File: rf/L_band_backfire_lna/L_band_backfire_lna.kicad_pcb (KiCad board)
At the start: 2 copper layers, 42.6 x 42.6 mm, 24 parts, among them J1 SMA, J2 SMA, U1 QPL9547, U2 QPL9547, X1 SAW, X2 SAW

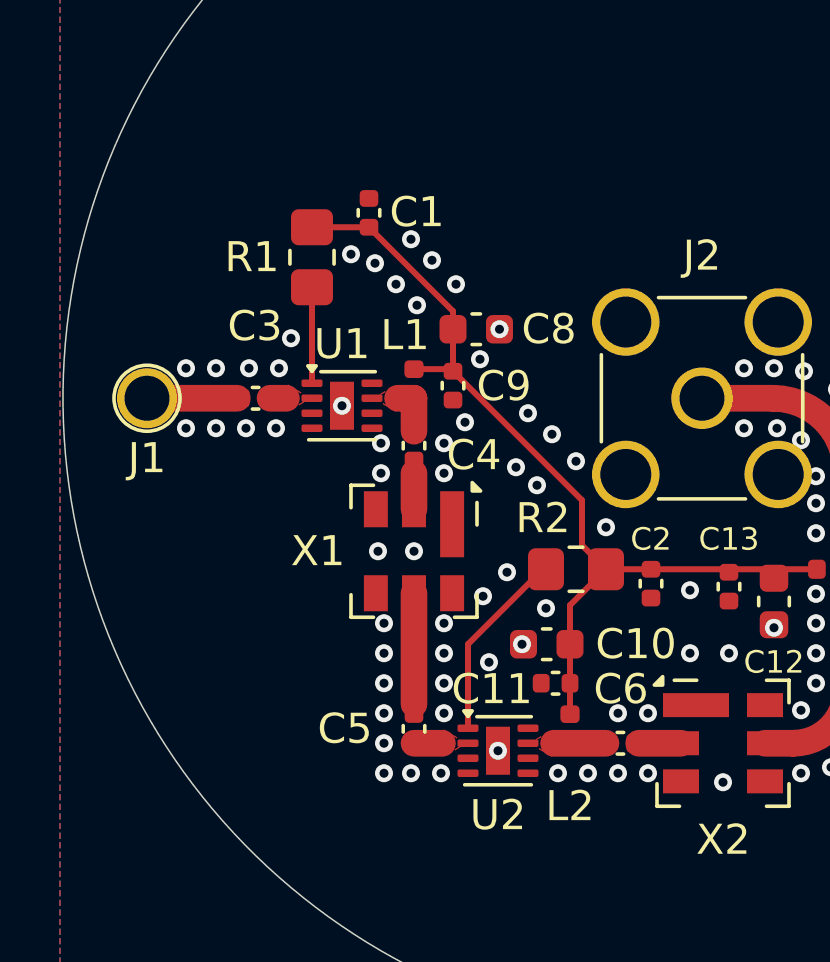
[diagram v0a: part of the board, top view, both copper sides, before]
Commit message: Make curves smoother
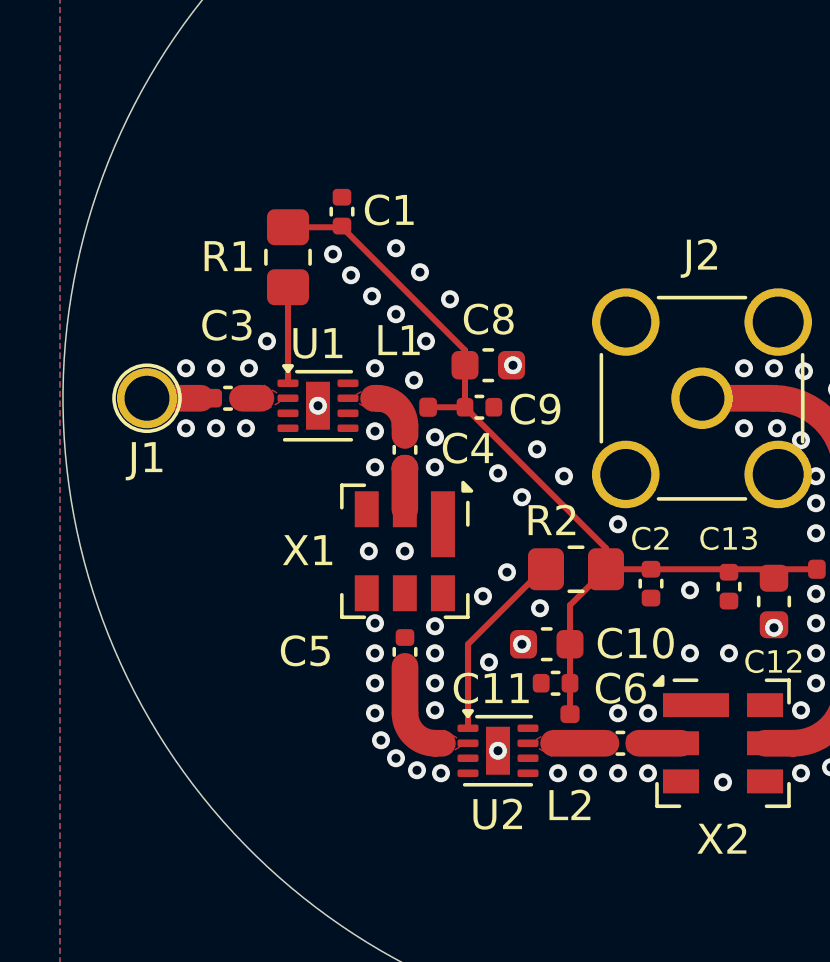
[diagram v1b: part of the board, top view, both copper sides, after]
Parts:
- moved C5 2.58 mm to (140.1, 108.5)
- moved C8 1.26 mm to (142.9, 98.9)
- moved C9 1.14 mm to (142.6, 100.3), turned to 180 degrees
- moved C3 0.92 mm to (134.2, 100.0)
- moved C1 0.90 mm to (138.0, 93.8)
- moved R1 0.80 mm to (136.2, 95.3)
- moved U1 0.80 mm to (137.2, 100.2)
- moved L1 0.79 mm to (140.4, 100.3), turned to 0 degrees
- moved C4 0.33 mm to (140.1, 101.7)
- moved X1 0.31 mm to (140.1, 105.1)
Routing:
- net Net-(X1-OUT): track 3.70 -> 0.00 mm
- net Net-(C5-Pad2): track 0.95 -> 3.34 mm
- net Net-(J1-In): track 3.01 -> 1.80 mm
- net GND: vias 90 -> 88

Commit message: idk
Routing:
- net GND: vias 88 -> 97
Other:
- board text added: "RFIN"
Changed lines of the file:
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@@
 		(tags "resistor handsolder")
 		(property "Reference" "R2"
-			(at 0.8 1.6 180)
+			(at 0.7 1.6 180)
 			(layer "F.SilkS")
 			(effects
@@
 		(tags "capacitor")
 		(property "Reference" "C6"
-			(at 0.02 -1.8 0)
+			(at 0.12 2.1 0)
 			(layer "F.SilkS")
 			(effects
@@
 	(footprint "Inductor_SMD:L_0402_1005Metric"
 		(layer "F.Cu")
-		(at 140.385 100.3)
+		(at 140.415 100.3)
 		(descr "Inductor SMD 0402 (1005 Metric), square (rectangular) end terminal, IPC-7351 nominal, (Body size source: http://www.tortai-tech.com/upload/download/2011102023233369053.pdf), generated with kicad-footprint-generator")
 		(tags "inductor")
@@
 		(tags "DFN NoLead")
 		(property "Reference" "U1"
-			(at 0 -2.05 0)
+			(at 0 1.95 0)
 			(layer "F.SilkS")
 			(effects
@@
 		(tags "capacitor")
 		(property "Reference" "C5"
-			(at 0 3.3 180)
+			(at 0 2.2 180)
 			(layer "F.SilkS")
 			(effects
@@
 			(at 0 -4.75 0)
 			(layer "F.SilkS")
+			(hide yes)
 			(effects
 				(font
@@
 		(tags "inductor")
 		(property "Reference" "L2"
-			(at -2.585 0 180)
+			(at -2.585 -0.3 180)
 			(layer "F.SilkS")
 			(effects
@@
 			(unlocked yes)
 			(layer "F.SilkS")
+			(hide yes)
 			(effects
 				(font
@@
 		(tags "capacitor")
 		(property "Reference" "C3"
-			(at -0.02 -2.4 0)
+			(at 0 -1.9 0)
 			(layer "F.SilkS")
 			(effects
@@
 		(tags "DFN NoLead")
 		(property "Reference" "U2"
-			(at 0 2.15 0)
+			(at -0.4 2.05 0)
 			(layer "F.SilkS")
 			(effects
@@
 		(layer "Edge.Cuts")
 	)
+	(gr_text "RFIN"
+		(at 129.5 102.7 0)
+		(layer "F.SilkS" knockout)
+		(effects
+			(font
+				(size 1 1)
+				(thickness 0.2)
+				(bold yes)
+			)
+			(justify left bottom)
+		)
+	)
 	(via
 		(at 151.4 101)
@@
 	)
 	(via
+		(at 144.7 110.5)
+		(size 0.6)
+		(drill 0.3)
+		(layers "F.Cu" "B.Cu")
+		(net 1)
+	)
+	(via
 		(at 143.7 98.9)
 		(size 0.6)
@@
 	)
 	(via
+		(at 149.6 106.5)
+		(size 0.6)
+		(drill 0.3)
+		(layers "F.Cu" "B.Cu")
+		(net 1)
+	)
+	(via
 		(at 150.7 112.8)
 		(size 0.6)
@@
 	)
 	(via
-		(at 147.2 110.5)
+		(at 147.3 110.5)
 		(size 0.6)
 		(drill 0.3)
@@
 	)
 	(via
-		(at 138.3 95.9)
+		(at 138.4 95.8)
 		(size 0.6)
 		(drill 0.3)
@@
 	)
 	(via
-		(at 139.1 99)
+		(at 146.5 110.500576)
+		(size 0.6)
+		(drill 0.3)
+		(layers "F.Cu" "B.Cu")
+		(net 1)
+	)
+	(via
+		(at 139.6 99)
 		(size 0.6)
 		(drill 0.3)
@@
 	)
 	(via
-		(at 135.5 98.1)
+		(at 135.5 97.6)
 		(size 0.6)
 		(drill 0.3)
@@
 	)
 	(via
-		(at 139 96.6)
+		(at 139.1 96.5)
 		(size 0.6)
 		(drill 0.3)
@@
 	)
 	(via
+		(at 135.5 98.5)
+		(size 0.6)
+		(drill 0.3)
+		(layers "F.Cu" "B.Cu")
+		(net 1)
+	)
+	(via
 		(at 141.1 107.6)
 		(size 0.6)
@@
 	)
 	(via
+		(at 138 92.6)
+		(size 0.6)
+		(drill 0.3)
+		(layers "F.Cu" "B.Cu")
+		(net 1)
+	)
+	(via
 		(at 139.1 109.5)
 		(size 0.6)
@@
 	)
 	(via
-		(at 149.6 106.4)
+		(at 149.6 107.5)
+		(size 0.6)
+		(drill 0.3)
+		(layers "F.Cu" "B.Cu")
+		(net 1)
+	)
+	(via
+		(at 150.9 107.5)
 		(size 0.6)
 		(drill 0.3)
@@
 	)
 	(via
-		(at 137.7 95.2)
+		(at 138.8 99)
+		(size 0.6)
+		(drill 0.3)
+		(layers "F.Cu" "B.Cu")
+		(net 1)
+	)
+	(via
+		(at 137.7 95.1)
 		(size 0.6)
 		(drill 0.3)
@@
 	)
 	(via
+		(at 136.9 97.6)
+		(size 0.6)
+		(drill 0.3)
+		(layers "F.Cu" "B.Cu")
+		(net 1)
+	)
+	(via
+		(at 136.9 98.5)
+		(size 0.6)
+		(drill 0.3)
+		(layers "F.Cu" "B.Cu")
+		(net 1)
+	)
+	(via
 		(at 138.895 105.1)
 		(size 0.6)
@@
 	)
 	(segment
-		(start 140.87 100.3)
+		(start 140.9 100.3)
 		(end 142.1 100.3)
 		(width 0.2)
@@
 	)
 	(segment
-		(start 140.1 100.918815)
+		(start 140.1 100.956277)
 		(end 140.1 101.24)
 		(width 0.8887)
@@
 	)
 	(segment
-		(start 139.181185 100)
+		(start 139.143723 100)
 		(end 139.052784 100)
 		(width 0.8887)
@@
 	)
 	(arc
-		(start 139.181185 100)
-		(mid 139.830885 100.269115)
-		(end 140.1 100.918815)
+		(start 139.143723 100)
+		(mid 139.819913 100.280087)
+		(end 140.1 100.956277)
 		(width 0.8887)
 		(layer "F.Cu")
@@
 		(polygon
 			(pts
-				(xy 138.8 104.4) (xy 138.8 101.2) (xy 137.8 101.2) (xy 137.8 98.7) (xy 140.120911 98.7) (xy 140.168503 98.704687)
-				(xy 140.2392 98.71875) (xy 140.34105 98.760938) (xy 140.400984 98.800984) (xy 140.531235 98.931235)
-				(xy 140.571596 98.980481) (xy 140.61151 99.040386) (xy 140.633938 99.082546) (xy 140.680647 99.196153)
-				(xy 140.694412 99.266809) (xy 140.698874 99.314354) (xy 140.696209 99.821544) (xy 140.683777 99.865012)
-				(xy 140.65608 99.909994) (xy 140.631167 99.932998) (xy 140.546834 99.976077) (xy 140.524469 99.996642)
-				(xy 140.505741 100.026775) (xy 140.499338 100.048644) (xy 140.493868 100.450817) (xy 140.499876 100.480211)
-				(xy 140.512943 100.523473) (xy 140.527967 100.560545) (xy 140.566705 100.635542) (xy 140.589823 100.661942)
-				(xy 140.634291 100.692968) (xy 140.677966 100.709746) (xy 141.145015 100.768128) (xy 141.189893 100.782264)
-				(xy 141.237477 100.807398) (xy 141.265208 100.829223) (xy 141.323389 100.89513) (xy 141.341865 100.920321)
-				(xy 141.366155 100.960621) (xy 141.391539 101.027732) (xy 141.4 101.074017) (xy 141.4 104.4)
+				(xy 138.8 104.4) (xy 138.8 101.2) (xy 137.8 101.2) (xy 137.8 99.441048) (xy 137.811704 99.368925)
+				(xy 137.846817 99.263587) (xy 137.880728 99.198864) (xy 137.906644 99.157807) (xy 138.022208 99.003722)
+				(xy 138.041791 98.980542) (xy 138.073184 98.947473) (xy 138.143673 98.888645) (xy 138.19454 98.85535)
+				(xy 138.229622 98.835189) (xy 138.363504 98.768248) (xy 138.439712 98.740625) (xy 138.558852 98.7125)
+				(xy 138.666209 98.7) (xy 140.120911 98.7) (xy 140.168503 98.704687) (xy 140.2392 98.71875) (xy 140.34105 98.760938)
+				(xy 140.400984 98.800984) (xy 140.531235 98.931235) (xy 140.571596 98.980481) (xy 140.61151 99.040386)
+				(xy 140.633938 99.082546) (xy 140.680647 99.196153) (xy 140.694412 99.266809) (xy 140.698874 99.314354)
+				(xy 140.696209 99.821544) (xy 140.683777 99.865012) (xy 140.65608 99.909994) (xy 140.631167 99.932998)
+				(xy 140.546834 99.976077) (xy 140.524469 99.996642) (xy 140.505741 100.026775) (xy 140.499338 100.048644)
+				(xy 140.493868 100.450817) (xy 140.499876 100.480211) (xy 140.512943 100.523473) (xy 140.527967 100.560545)
+				(xy 140.566705 100.635542) (xy 140.589823 100.661942) (xy 140.634291 100.692968) (xy 140.677966 100.709746)
+				(xy 141.145015 100.768128) (xy 141.189893 100.782264) (xy 141.237477 100.807398) (xy 141.265208 100.829223)
+				(xy 141.323389 100.89513) (xy 141.341865 100.920321) (xy 141.366155 100.960621) (xy 141.391539 101.027732)
+				(xy 141.4 101.074017) (xy 141.4 104.4)
 			)
 		)
@@
 		(polygon
 			(pts
-				(xy 143.8 112.8) (xy 150 112.8) (xy 150 110.2) (xy 146 110.2) (xy 145.1 110.2) (xy 143.8 110.2)
+				(xy 143.8 112.8) (xy 150 112.8) (xy 150 110.2) (xy 146 110.2) (xy 145.1 110.2) (xy 144.63563 110.2)
+				(xy 144.518985 110.223202) (xy 144.387565 110.277638) (xy 144.31798 110.314832) (xy 144.243815 110.364388)
+				(xy 144.209506 110.392545) (xy 144.187609 110.412391) (xy 144.122676 110.477324) (xy 144.079388 110.520612)
+				(xy 144.014455 110.585545) (xy 143.988995 110.613636) (xy 143.952873 110.657651) (xy 143.905191 110.729011)
+				(xy 143.878351 110.779226) (xy 143.833271 110.888058) (xy 143.816743 110.942544) (xy 143.804186 111.005675)
+				(xy 143.8 111.048173)
 			)
 		)
